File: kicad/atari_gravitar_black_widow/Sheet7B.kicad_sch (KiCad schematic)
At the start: 37 parts, among them Q10 2N3904, Q5 2N3904, Q6 2N3904, Q7 2N3906, Q8 2N3904, Q9 2N3904

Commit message: traces and more traces
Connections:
- net Z_OUT: no longer Q5.3 (C), Q7.1 (E), Q9.2 (B), R149.1, R152.1, R153.2, R156.1
- net at R157.2: no longer Q9.1 (E)
- new net: Q5.3 (C), Q7.1 (E), Q9.2 (B), R149.1, R152.1, R153.2, R156.1
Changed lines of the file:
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@@
   (junction (at 521.208 128.397) (diameter 0) (color 0 0 0 0)
   )
-  (junction (at 223.139 265.684) (diameter 0) (color 0 0 0 0)
-  )
   (junction (at 424.307 222.631) (diameter 0) (color 0 0 0 0)
   )
@@
   (junction (at 187.96 239.268) (diameter 0) (color 0 0 0 0)
   )
+  (junction (at 242.1128 265.684) (diameter 0) (color 0 0 0 0)
+  )
   (junction (at 215.011 295.148) (diameter 0) (color 0 0 0 0)
   )
@@
   )
   (junction (at 521.208 196.723) (diameter 0) (color 0 0 0 0)
+  )
+  (junction (at 515.24 265.68) (diameter 0) (color 0 0 0 0)
   )
   (junction (at 205.74 295.148) (diameter 0) (color 0 0 0 0)
@@
     (stroke (width 0) (type default) (color 0 0 0 0))
   )
-  (wire (pts (xy 223.139 265.684) (xy 515.239 265.684))
-    (stroke (width 0) (type default) (color 0 0 0 0))
-  )
   (wire (pts (xy 140.843 223.393) (xy 144.78 223.393))
     (stroke (width 0) (type default) (color 0 0 0 0))
@@
     (stroke (width 0) (type default) (color 0 0 0 0))
   )
-  (wire (pts (xy 223.139 241.173) (xy 223.139 265.684))
-    (stroke (width 0) (type default) (color 0 0 0 0))
-  )
   (wire (pts (xy 351.155 220.091) (xy 355.219 220.091))
     (stroke (width 0) (type default) (color 0 0 0 0))
@@
     (stroke (width 0) (type default) (color 0 0 0 0))
   )
+  (wire (pts (xy 515.24 265.68) (xy 242.11 265.68))
+    (stroke (width 0) (type default) (color 0 0 0 0))
+  )
   (wire (pts (xy 91.694 227.203) (xy 94.488 227.203))
     (stroke (width 0) (type default) (color 0 0 0 0))
@@
     (stroke (width 0) (type default) (color 0 0 0 0))
   )
-  (wire (pts (xy 223.139 265.684) (xy 223.139 275.59))
+  (wire (pts (xy 223.139 241.173) (xy 223.139 275.59))
     (stroke (width 0) (type default) (color 0 0 0 0))
   )
@@
     (stroke (width 0) (type default) (color 0 0 0 0))
   )
+  (wire (pts (xy 242.11 265.68) (xy 242.11 265.69))
+    (stroke (width 0) (type default) (color 0 0 0 0))
+  )
   (wire (pts (xy 370.459 222.631) (xy 424.307 222.631))
     (stroke (width 0) (type default) (color 0 0 0 0))
@@
     (stroke (width 0) (type default) (color 0 0 0 0))
   )
+  (wire (pts (xy 242.062 264.0076) (xy 242.1128 246.2784))
+    (stroke (width 0) (type default) (color 0 0 0 0))
+  )
   (wire (pts (xy 313.563 210.312) (xy 283.845 210.312))
     (stroke (width 0) (type default) (color 0 0 0 0))
@@
     (stroke (width 0) (type default) (color 0 0 0 0))
   )
+  (wire (pts (xy 242.062 264.0076) (xy 242.1128 265.684))
+    (stroke (width 0) (type default) (color 0 0 0 0))
+  )
   (wire (pts (xy 397.256 249.428) (xy 397.256 261.493))
     (stroke (width 0) (type default) (color 0 0 0 0))
@@
   )
   (wire (pts (xy 94.488 227.203) (xy 94.488 229.743))
+    (stroke (width 0) (type default) (color 0 0 0 0))
+  )
+  (wire (pts (xy 230.7844 246.2784) (xy 242.1128 246.2784))
     (stroke (width 0) (type default) (color 0 0 0 0))
   )
@@
     (pin "3")
   )
-  (symbol (lib_id "power:GND") (at 230.759 253.873 0) (unit 1)
-    (in_bom yes) (on_board yes)
-    (property "Reference" "#PWR0340" (id 0) (at 230.759 260.223 0)
-      (effects (font (size 1.27 1.27)) hide)
-    )
-    (property "Value" "GND" (id 1) (at 234.569 255.778 0))
-    (property "Footprint" "" (id 2) (at 230.759 253.873 0)
-      (effects (font (size 1.27 1.27)) hide)
-    )
-    (property "Datasheet" "" (id 3) (at 230.759 253.873 0)
+  (symbol (lib_id "power:GND") (at 230.7844 253.8984 0) (unit 1)
+    (in_bom yes) (on_board yes)
+    (property "Reference" "#PWR0340" (id 0) (at 230.7844 260.2484 0)
+      (effects (font (size 1.27 1.27)) hide)
+    )
+    (property "Value" "GND" (id 1) (at 234.5944 255.8034 0))
+    (property "Footprint" "" (id 2) (at 230.7844 253.8984 0)
+      (effects (font (size 1.27 1.27)) hide)
+    )
+    (property "Datasheet" "" (id 3) (at 230.7844 253.8984 0)
       (effects (font (size 1.27 1.27)) hide)
     )
@@
     (pin "1")
   )
-  (symbol (lib_id "Device:R_US") (at 230.759 250.063 180) (unit 1)
-    (in_bom yes) (on_board yes) (fields_autoplaced)
-    (property "Reference" "R157" (id 0) (at 232.41 249.1545 0)
+  (symbol (lib_id "Device:R_US") (at 230.7844 250.0884 180) (unit 1)
+    (in_bom yes) (on_board yes)
+    (property "Reference" "R157" (id 0) (at 233.5276 249.0724 0)
       (effects (font (size 1.27 1.27)) (justify right))
     )
-    (property "Value" "27" (id 1) (at 232.41 251.9296 0)
+    (property "Value" "27" (id 1) (at 232.4354 251.955 0)
       (effects (font (size 1.27 1.27)) (justify right))
     )
-    (property "Footprint" "Star_Wars_Vector_PCB:GenericComp" (id 2) (at 229.743 249.809 90)
-      (effects (font (size 1.27 1.27)) hide)
-    )
-    (property "Datasheet" "~" (id 3) (at 230.759 250.063 0)
-      (effects (font (size 1.27 1.27)) hide)
-    )
+    (property "Footprint" "Star_Wars_Vector_PCB:GenericComp" (id 2) (at 229.7684 249.8344 90)
+      (effects (font (size 1.27 1.27)) hide)
+    )
+    (property "Datasheet" "~" (id 3) (at 230.7844 250.0884 0)
+      (effects (font (size 1.27 1.27)) hide)
+    )

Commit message: zout
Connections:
- net Z_OUT: now also Q9.1 (E), R157.2
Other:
- moved on the sheet: R157

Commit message: more traces
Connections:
- net Z_OUT: no longer Q9.1 (E), R157.2, TPZOUT1.1, TPZOUT1.2
- new net: Q9.1 (E), R157.2, TPZOUT1.1, TPZOUT1.2
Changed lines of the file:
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@@
   (junction (at 205.74 295.148) (diameter 0) (color 0 0 0 0)
-  )
-  (junction (at 515.239 196.723) (diameter 0) (color 0 0 0 0)
   )
   (no_connect (at 121.793 255.143))
@@
   (no_connect (at 91.694 234.823))
   (no_connect (at 313.563 202.692))
-  (wire (pts (xy 515.239 196.723) (xy 515.239 177.546))
-    (stroke (width 0) (type default) (color 0 0 0 0))
-  )
   (polyline (pts (xy 240.411 235.458) (xy 240.411 259.08))
     (stroke (width 0) (type default) (color 0 0 0 0))
@@
     (stroke (width 0) (type default) (color 0 0 0 0))
   )
-  (wire (pts (xy 515.239 177.546) (xy 522.732 177.546))
-    (stroke (width 0) (type default) (color 0 0 0 0))
-  )

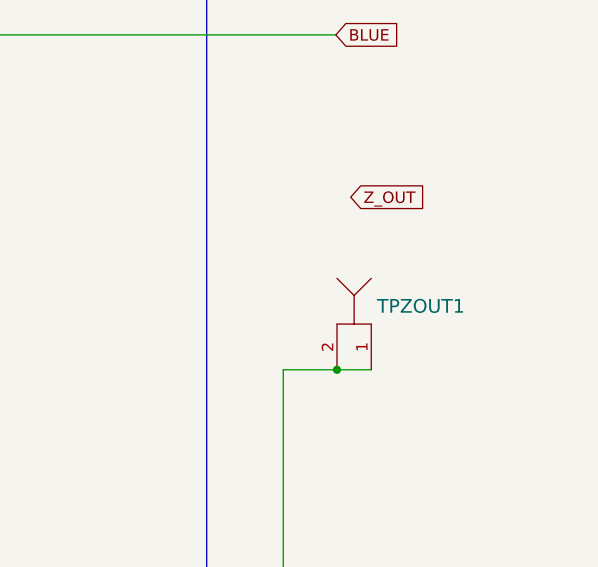
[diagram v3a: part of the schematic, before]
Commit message: Row 3 - 3.5 tracess
Also fixed some schematic errors (IO at J6, power at R4, Z out TP)
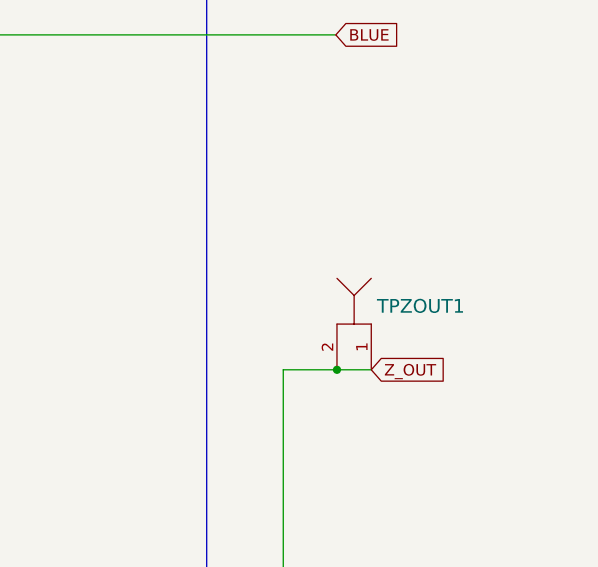
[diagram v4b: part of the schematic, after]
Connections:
- net Z_OUT: now also Q9.1 (E), R157.2, TPZOUT1.1, TPZOUT1.2
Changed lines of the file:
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@@
     )
   )
-  (global_label "Z_OUT" (shape input) (at 522.732 177.546 0) (fields_autoplaced)
+  (global_label "Z_OUT" (shape input) (at 525.018 196.723 0) (fields_autoplaced)
     (effects (font (size 1.27 1.27)) (justify left))
-    (property "Intersheet References" "${INTERSHEET_REFS}" (id 0) (at 530.8619 177.4666 0)
+    (property "Intersheet References" "${INTERSHEET_REFS}" (id 0) (at 533.1479 196.6436 0)
       (effects (font (size 1.27 1.27)) (justify left) hide)
     )

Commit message: lots o' traces
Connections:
- net GND: now also F_6.15 (E)
- no-connect marks 17 -> 16
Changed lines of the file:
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@@
   (junction (at 205.74 295.148) (diameter 0) (color 0 0 0 0)
   )
-  (no_connect (at 121.793 255.143))
   (no_connect (at 346.583 198.882))
   (no_connect (at 346.583 201.422))
@@
     (pin "2")
   )
+  (symbol (lib_id "power:GND") (at 121.793 255.143 0) (unit 1)
+    (in_bom yes) (on_board yes)
+    (property "Reference" "#PWR0266" (id 0) (at 121.793 261.493 0)
+      (effects (font (size 1.27 1.27)) hide)
+    )
+    (property "Value" "GND" (id 1) (at 125.603 257.048 0))
+    (property "Footprint" "" (id 2) (at 121.793 255.143 0)
+      (effects (font (size 1.27 1.27)) hide)
+    )
+    (property "Datasheet" "" (id 3) (at 121.793 255.143 0)
+      (effects (font (size 1.27 1.27)) hide)
+    )
+    (pin "1")
+  )
   (symbol (lib_id "power:+5V") (at 87.122 270.383 180) (unit 1)

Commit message: second to last cleanup?
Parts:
- C118: value .1uf -> 220pf
- R150: value 22k -> 1k
- R57: value 4.7k -> 2.2k
- R58: value 4.7k -> 10k
- R59: value 4.7k -> 1.2k
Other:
- note added: "Atari schematic shows /Z0 but it is Z0"
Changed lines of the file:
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@@
   (junction (at 530.479 133.858) (diameter 0) (color 0 0 0 0)
   )
-  (junction (at 352.679 211.582) (diameter 0) (color 0 0 0 0)
-  )
   (junction (at 230.759 247.523) (diameter 0) (color 0 0 0 0)
   )
@@
   (junction (at 215.011 295.148) (diameter 0) (color 0 0 0 0)
   )
-  (junction (at 355.346 238.887) (diameter 0) (color 0 0 0 0)
-  )
-  (junction (at 352.679 225.171) (diameter 0) (color 0 0 0 0)
+  (junction (at 352.6878 238.887) (diameter 0) (color 0 0 0 0)
   )
   (junction (at 187.96 224.028) (diameter 0) (color 0 0 0 0)
@@
   )
   (junction (at 187.96 229.108) (diameter 0) (color 0 0 0 0)
+  )
+  (junction (at 352.6904 225.171) (diameter 0) (color 0 0 0 0)
   )
   (junction (at 407.162 174.625) (diameter 0) (color 0 0 0 0)
@@
     (stroke (width 0) (type default) (color 0 0 0 0))
   )
-  (wire (pts (xy 352.679 225.171) (xy 355.219 225.171))
+  (wire (pts (xy 352.679 225.171) (xy 352.6904 225.171))
     (stroke (width 0) (type default) (color 0 0 0 0))
   )
@@
     (stroke (width 0) (type default) (color 0 0 0 0))
   )
+  (wire (pts (xy 352.6878 238.887) (xy 355.346 238.887))
+    (stroke (width 0) (type default) (color 0 0 0 0))
+  )
   (wire (pts (xy 205.613 308.229) (xy 207.391 308.229))
     (stroke (width 0) (type default) (color 0 0 0 0))
@@
     (stroke (width 0) (type default) (color 0 0 0 0))
   )
+  (wire (pts (xy 352.6904 225.171) (xy 355.219 225.171))
+    (stroke (width 0) (type default) (color 0 0 0 0))
+  )
   (wire (pts (xy 165.735 306.705) (xy 165.735 305.689))
     (stroke (width 0) (type default) (color 0 0 0 0))
@@
     (stroke (width 0) (type default) (color 0 0 0 0))
   )
-  (wire (pts (xy 343.027 256.159) (xy 355.346 256.159))
+  (wire (pts (xy 343.027 256.159) (xy 352.6878 256.159))
     (stroke (width 0) (type default) (color 0 0 0 0))
   )
@@
     (stroke (width 0) (type default) (color 0 0 0 0))
   )
-  (wire (pts (xy 355.219 211.582) (xy 352.679 211.582))
-    (stroke (width 0) (type default) (color 0 0 0 0))
-  )
   (wire (pts (xy 203.962 308.229) (xy 205.613 308.229))
     (stroke (width 0) (type default) (color 0 0 0 0))
@@
     (stroke (width 0) (type default) (color 0 0 0 0))
   )
-  (wire (pts (xy 352.679 211.582) (xy 352.679 225.171))
-    (stroke (width 0) (type default) (color 0 0 0 0))
-  )
   (wire (pts (xy 40.386 227.203) (xy 56.134 227.203))
     (stroke (width 0) (type default) (color 0 0 0 0))
@@
     (stroke (width 0) (type default) (color 0 0 0 0))
   )
-  (wire (pts (xy 352.679 211.582) (xy 352.552 211.582))
-    (stroke (width 0) (type default) (color 0 0 0 0))
-  )
   (wire (pts (xy 99.822 237.363) (xy 99.822 244.602))
     (stroke (width 0) (type default) (color 0 0 0 0))
@@
     (stroke (width 0) (type default) (color 0 0 0 0))
   )
+  (wire (pts (xy 352.6904 211.582) (xy 355.219 211.582))
+    (stroke (width 0) (type default) (color 0 0 0 0))
+  )
   (wire (pts (xy 187.96 249.301) (xy 204.089 249.301))
     (stroke (width 0) (type default) (color 0 0 0 0))
@@
     (stroke (width 0) (type default) (color 0 0 0 0))
   )
-  (wire (pts (xy 355.346 256.159) (xy 355.346 238.887))
+  (wire (pts (xy 352.6878 256.159) (xy 352.6878 238.887))
     (stroke (width 0) (type default) (color 0 0 0 0))
   )
@@
     (stroke (width 0) (type default) (color 0 0 0 0))
   )
+  (wire (pts (xy 352.6904 225.171) (xy 352.6904 211.582))
+    (stroke (width 0) (type default) (color 0 0 0 0))
+  )
   (wire (pts (xy 40.513 200.533) (xy 102.743 200.533))
     (stroke (width 0) (type default) (color 0 0 0 0))
@@
     (stroke (width 0) (type default) (color 0 0 0 0))
   )
-  (wire (pts (xy 352.679 238.887) (xy 355.346 238.887))
+  (wire (pts (xy 352.679 238.887) (xy 352.6878 238.887))
     (stroke (width 0) (type default) (color 0 0 0 0))
   )
@@
   (text "NOT LOADED\n" (at 226.822 258.953 0)
     (effects (font (size 1.27 1.27) (thickness 0.508) bold) (justify left bottom))
+  )
+  (text "Atari schematic\nshows /Z0 but\nit is Z0" (at 17.1514 272.5379 0)
+    (effects (font (size 1.27 1.27)) (justify left bottom))
   )
   (global_label "~{Z1}" (shape input) (at 40.64 265.303 180) (fields_autoplaced)
@@
   (symbol (lib_id "Device:R_US") (at 184.15 239.268 270) (unit 1)
     (in_bom yes) (on_board yes)
-    (property "Reference" "R58" (id 0) (at 184.023 241.173 90))
-    (property "Value" "4.7k" (id 1) (at 184.15 237.1876 90))
+    (property "Reference" "R58" (id 0) (at 184.0216 237.7669 90))
+    (property "Value" "10k" (id 1) (at 183.9917 240.7343 90))
     (property "Footprint" "Star_Wars_Vector_PCB:GenericComp" (id 2) (at 183.896 240.284 90)
       (effects (font (size 1.27 1.27)) hide)
@@
   )
   (symbol (lib_id "Device:R_US") (at 209.677 295.148 270) (unit 1)
-    (in_bom yes) (on_board yes) (fields_autoplaced)
-    (property "Reference" "R150" (id 0) (at 209.677 290.2925 90))
-    (property "Value" "22k" (id 1) (at 209.677 293.0676 90))
+    (in_bom yes) (on_board yes)
+    (property "Reference" "R150" (id 0) (at 209.6794 292.6922 90))
+    (property "Value" "1k" (id 1) (at 209.7035 298.0392 90))
     (property "Footprint" "Star_Wars_Vector_PCB:GenericComp" (id 2) (at 209.423 296.164 90)
       (effects (font (size 1.27 1.27)) hide)
@@
   (symbol (lib_id "Device:R_US") (at 184.15 229.108 270) (unit 1)
     (in_bom yes) (on_board yes)
-    (property "Reference" "R57" (id 0) (at 184.15 230.759 90))
-    (property "Value" "4.7k" (id 1) (at 184.15 227.076 90))
+    (property "Reference" "R57" (id 0) (at 184.1414 227.4656 90))
+    (property "Value" "2.2k" (id 1) (at 184.1655 231.0066 90))
     (property "Footprint" "Star_Wars_Vector_PCB:GenericComp" (id 2) (at 183.896 230.124 90)
       (effects (font (size 1.27 1.27)) hide)
@@
   (symbol (lib_id "Device:C") (at 211.201 308.229 90) (unit 1)
     (in_bom yes) (on_board yes)
-    (property "Reference" "C118" (id 0) (at 210.0326 305.308 90)
+    (property "Reference" "C118" (id 0) (at 213.7062 304.8846 90)
       (effects (font (size 1.27 1.27)) (justify left))
     )
-    (property "Value" ".1uf" (id 1) (at 209.55 310.007 90)
+    (property "Value" "220pf" (id 1) (at 214.0087 311.8424 90)
       (effects (font (size 1.27 1.27)) (justify left))
     )
@@
   (symbol (lib_id "Device:R_US") (at 184.15 234.188 270) (unit 1)
     (in_bom yes) (on_board yes)
-    (property "Reference" "R56" (id 0) (at 184.023 236.093 90))
-    (property "Value" "4.7k" (id 1) (at 184.15 232.1076 90))
+    (property "Reference" "R56" (id 0) (at 184.2601 232.712 90))
+    (property "Value" "4.7k" (id 1) (at 183.8128 235.7986 90))
     (property "Footprint" "Star_Wars_Vector_PCB:GenericComp" (id 2) (at 183.896 235.204 90)
       (effects (font (size 1.27 1.27)) hide)
@@
   (symbol (lib_id "Device:R_US") (at 184.15 224.028 270) (unit 1)
     (in_bom yes) (on_board yes)
-    (property "Reference" "R59" (id 0) (at 183.007 225.679 90)
+    (property "Reference" "R59" (id 0) (at 182.2144 222.1662 90)
       (effects (font (size 1.27 1.27)) (justify left))
     )
-    (property "Value" "4.7k" (id 1) (at 182.118 221.742 90)
-      (effects (font (size 1.27 1.27)) (justify left))
+    (property "Value" "1.2k" (id 1) (at 182.0457 225.8035 90)
+      (effects (font (size 1 1)) (justify left))
     )
     (property "Footprint" "Star_Wars_Vector_PCB:GenericComp" (id 2) (at 183.896 225.044 90)
